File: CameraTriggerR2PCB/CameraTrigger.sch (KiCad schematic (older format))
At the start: 0 parts

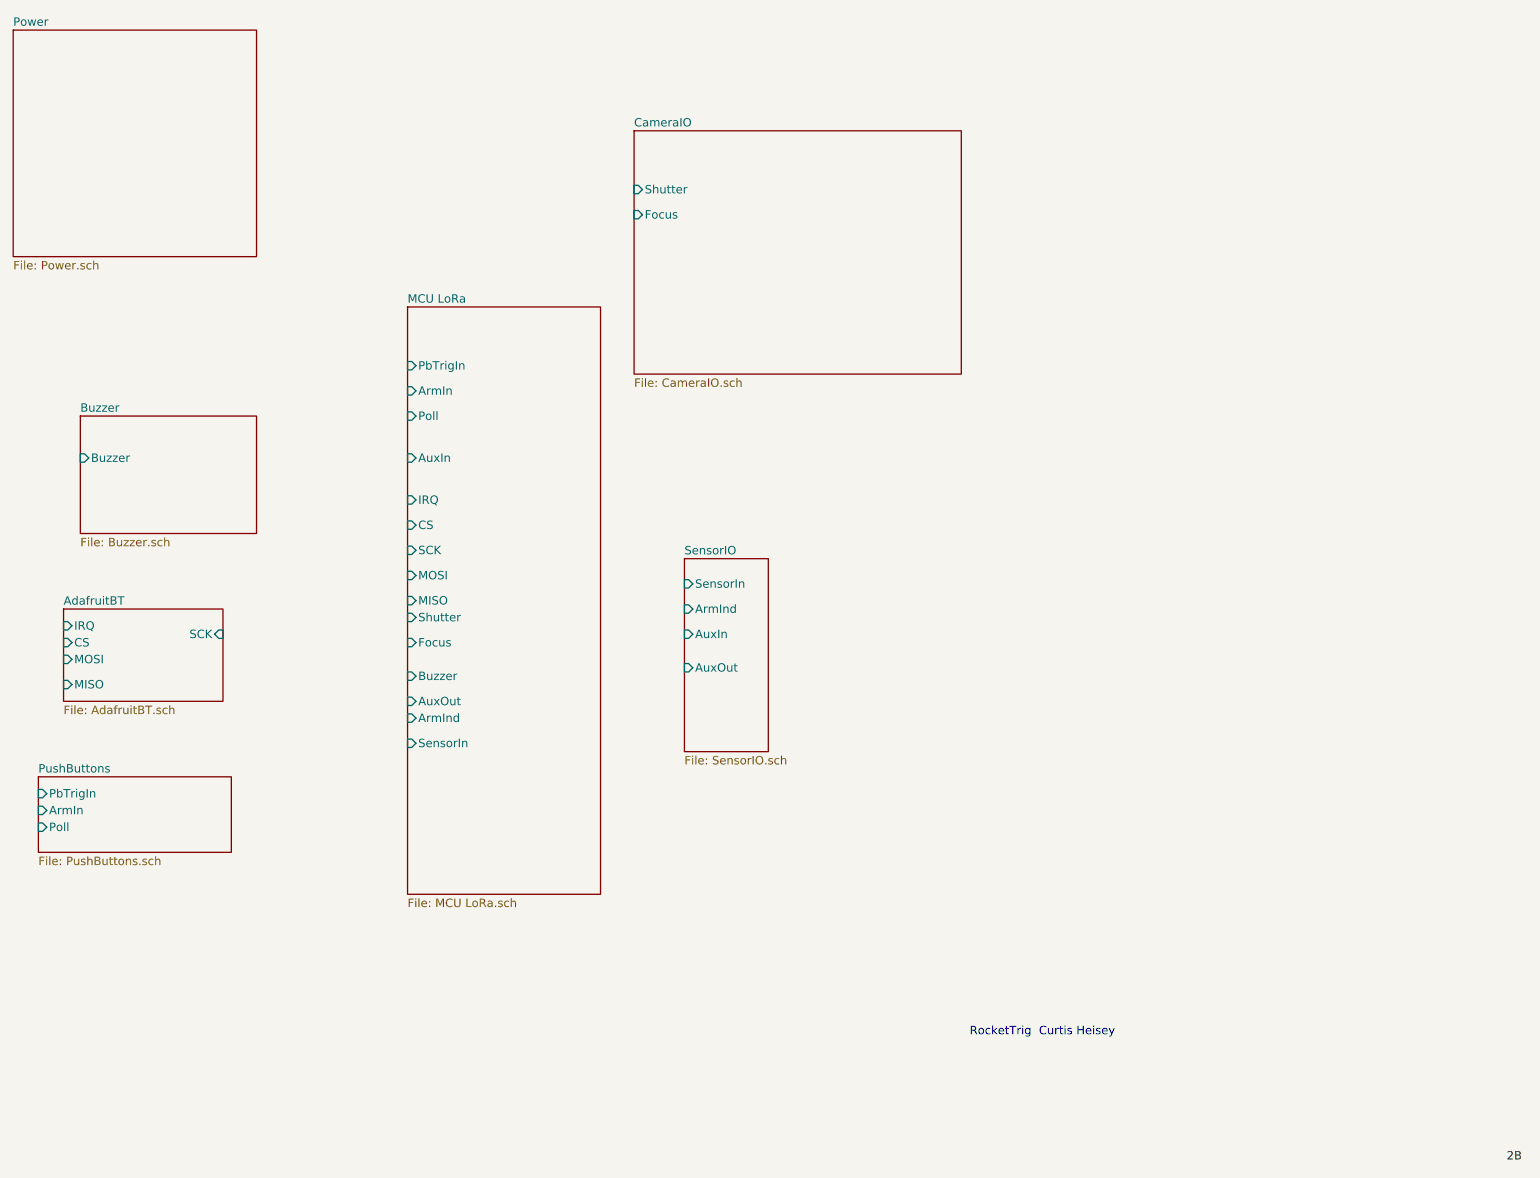
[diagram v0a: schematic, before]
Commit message: Add files via upload
Adding XLR connector
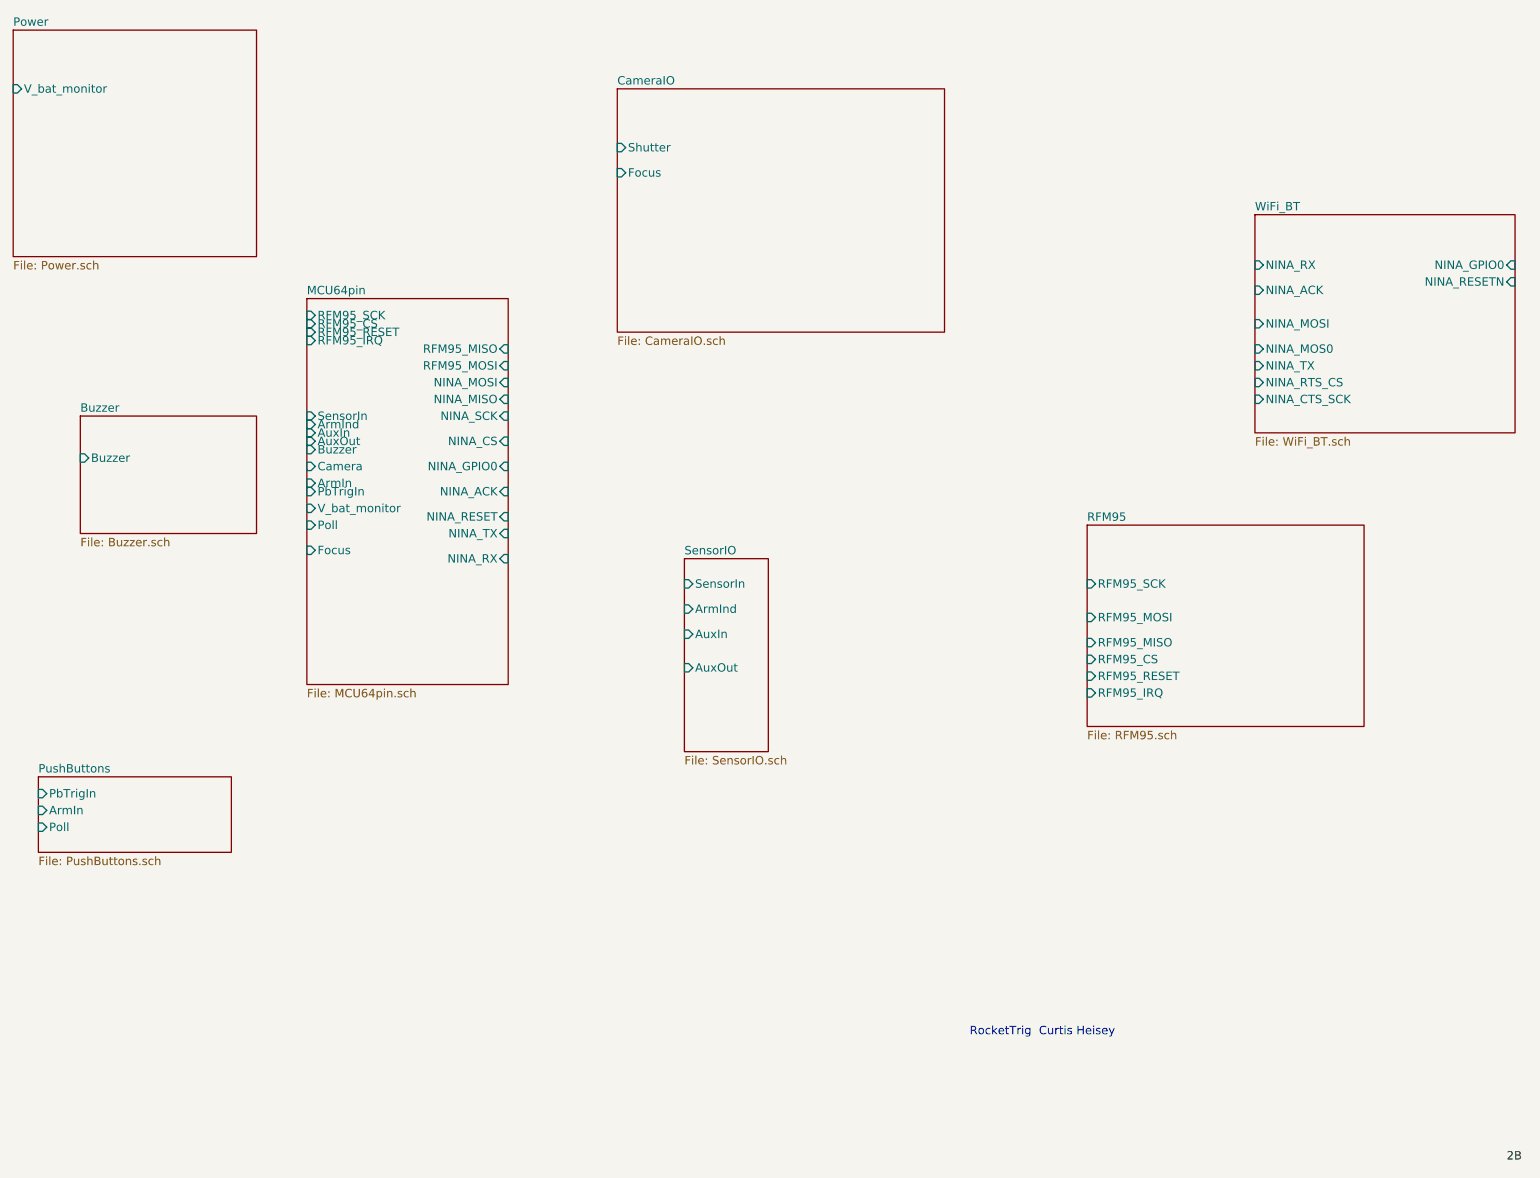
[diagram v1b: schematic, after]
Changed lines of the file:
@@
 $Descr A4 11693 8268
 encoding utf-8
-Sheet 1 8
+Sheet 1 9
 Title ""
 Date ""
@@
 RocketTrig  Curtis Heisey
 $Sheet
-S 5500 1500 1950 1450
+S 5400 1250 1950 1450
 U 5EBC562C
 F0 "CameraIO" 50
 F1 "CameraIO.sch" 50
-F2 "Shutter" I L 5500 1850 50
-F3 "Focus" I L 5500 2000 50
+F2 "Shutter" I L 5400 1600 50
+F3 "Focus" I L 5400 1750 50
 $EndSheet
 $Sheet
@@
 F0 "Power" 50
 F1 "Power.sch" 50
+F2 "V_bat_monitor" I L 1800 1250 50
 $EndSheet
 $Sheet
@@
 $EndSheet
 $Sheet
-S 2100 4350 950  550
-U 5ECB0F2B
-F0 "AdafruitBT" 50
-F1 "AdafruitBT.sch" 50
-F2 "IRQ" I L 2100 4450 50
-F3 "CS" I L 2100 4550 50
-F4 "MOSI" I L 2100 4650 50
-F5 "MISO" I L 2100 4800 50
-F6 "SCK" I R 3050 4500 50
-$EndSheet
-$Sheet
-S 4150 2550 1150 3500
-U 5ECB134F
-F0 "MCU LoRa" 50
-F1 "MCU LoRa.sch" 50
-F2 "PbTrigIn" I L 4150 2900 50
-F3 "ArmIn" I L 4150 3050 50
-F4 "Poll" I L 4150 3200 50
-F5 "AuxIn" I L 4150 3450 50
-F6 "IRQ" I L 4150 3700 50
-F7 "CS" I L 4150 3850 50
-F8 "SCK" I L 4150 4000 50
-F9 "MOSI" I L 4150 4150 50
-F10 "MISO" I L 4150 4300 50
-F11 "Shutter" I L 4150 4400 50
-F12 "Focus" I L 4150 4550 50
-F13 "Buzzer" I L 4150 4750 50
-F14 "AuxOut" I L 4150 4900 50
-F15 "ArmInd" I L 4150 5000 50
-F16 "SensorIn" I L 4150 5150 50
-$EndSheet
-$Sheet
 S 2200 3200 1050 700
 U 5ECC61B0
@@
 F2 "Buzzer" I L 2200 3450 50
 $EndSheet
+$Sheet
+S 8200 3850 1650 1200
+U 5EBC71CE
+F0 "RFM95" 50
+F1 "RFM95.sch" 50
+F2 "RFM95_SCK" I L 8200 4200 50
+F3 "RFM95_MOSI" I L 8200 4400 50
+F4 "RFM95_MISO" I L 8200 4550 50
+F5 "RFM95_CS" I L 8200 4650 50
+F6 "RFM95_RESET" I L 8200 4750 50
+F7 "RFM95_IRQ" I L 8200 4850 50
+$EndSheet
+$Sheet
+S 9200 2000 1550 1300
+U 5EBC729C
+F0 "WiFi_BT" 50
+F1 "WiFi_BT.sch" 50
+F2 "NINA_RX" I L 9200 2300 50
+F3 "NINA_ACK" I L 9200 2450 50
+F4 "NINA_MOSI" I L 9200 2650 50
+F5 "NINA_MOS0" I L 9200 2800 50
+F6 "NINA_TX" I L 9200 2900 50
+F7 "NINA_RTS_CS" I L 9200 3000 50
+F8 "NINA_CTS_SCK" I L 9200 3100 50
+F9 "NINA_GPIO0" I R 10750 2300 50
+F10 "NINA_RESETN" I R 10750 2400 50
+$EndSheet
+$Sheet
+S 3550 2500 1200 2300
+U 5EBF5198
+F0 "MCU64pin" 50
+F1 "MCU64pin.sch" 50
+F2 "RFM95_SCK" I L 3550 2600 50
+F3 "RFM95_CS" I L 3550 2650 50
+F4 "RFM95_RESET" I L 3550 2700 50
+F5 "RFM95_IRQ" I L 3550 2750 50
+F6 "SensorIn" I L 3550 3200 50
+F7 "ArmInd" I L 3550 3250 50
+F8 "AuxIn" I L 3550 3300 50
+F9 "AuxOut" I L 3550 3350 50
+F10 "Buzzer" I L 3550 3400 50
+F11 "Camera" I L 3550 3500 50
+F12 "PbTrigIn" I L 3550 3650 50
+F13 "ArmIn" I L 3550 3600 50
+F14 "Poll" I L 3550 3850 50
+F15 "V_bat_monitor" I L 3550 3750 50
+F16 "RFM95_MISO" I R 4750 2800 50
+F17 "RFM95_MOSI" I R 4750 2900 50
+F18 "Focus" I L 3550 4000 50
+F19 "NINA_MOSI" I R 4750 3000 50
+F20 "NINA_MISO" I R 4750 3100 50
+F21 "NINA_SCK" I R 4750 3200 50
+F22 "NINA_CS" I R 4750 3350 50
+F23 "NINA_GPIO0" I R 4750 3500 50
+F24 "NINA_ACK" I R 4750 3650 50
+F25 "NINA_RESET" I R 4750 3800 50
+F26 "NINA_TX" I R 4750 3900 50
+F27 "NINA_RX" I R 4750 4050 50
+$EndSheet
 $EndSCHEMATC
